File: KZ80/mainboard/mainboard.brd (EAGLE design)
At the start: 100 x 80 mm, 32 parts, among them J1 RESET, J2 PWR/CLK

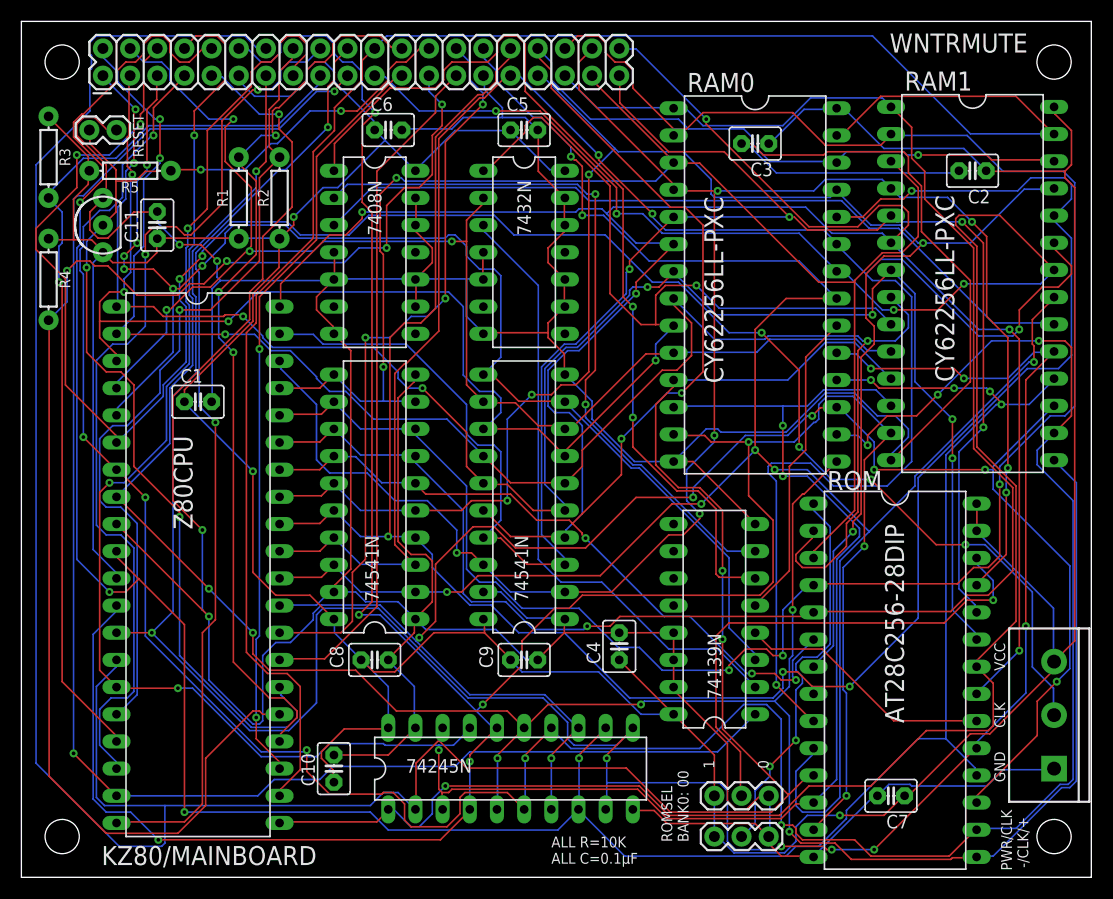
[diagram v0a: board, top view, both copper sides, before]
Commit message: mainboard: move RAM around
This moves the RAM chips to give more clearance to the ROM chip, e.g
to make swappung it out easier.
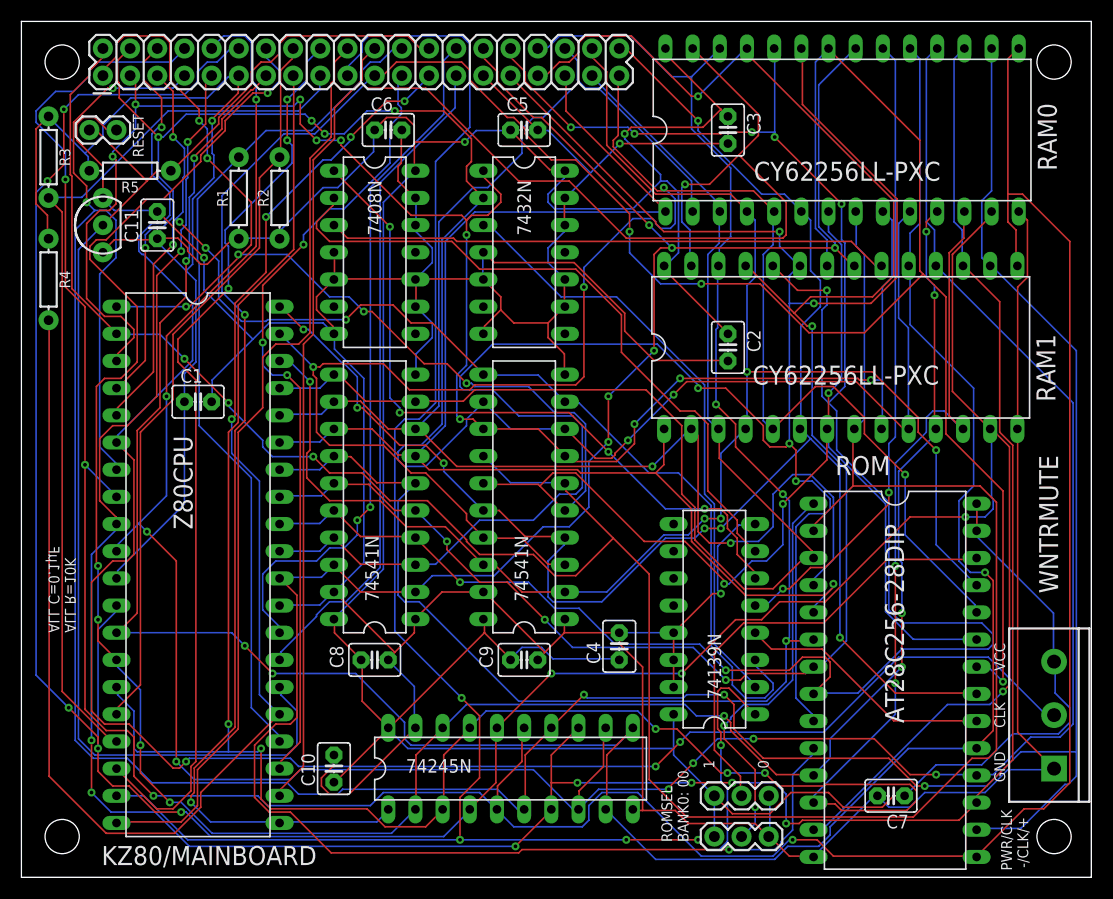
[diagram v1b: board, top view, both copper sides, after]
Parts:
- moved C2 28.2 mm to (66.0, 49.5), turned to 270 degrees
- moved RAM0 16.6 mm to (76.7, 69.8), turned to 0 degrees
- moved RAM1 13.7 mm to (76.6, 49.5), turned to 0 degrees
- moved C3 2.84 mm to (66.0, 69.8), turned to 270 degrees
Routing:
- net A12: track 159.5 -> 233.1 mm, vias 4 -> 3
- net A14: track 130.2 -> 184.2 mm, vias 4 -> 7
- net D0: track 268.7 -> 218.8 mm, vias 2 -> 10
- net A10: track 205.6 -> 156.8 mm, vias 5 -> 7
- net A6: track 187.6 -> 141.3 mm, vias 3 -> 2
- net D3: track 232.2 -> 275.2 mm, vias 7 -> 4
- net RD: track 214.0 -> 256.2 mm
- net GND: track 472.0 -> 431.0 mm, vias 2 -> 3
- net D4: track 253.0 -> 292.7 mm, vias 9 -> 5
- net A5: track 166.0 -> 128.6 mm
- net N$5: track 29.3 -> 59.8 mm, vias 0 -> 2
- net A11: track 169.3 -> 195.1 mm, vias 8 -> 9
- net MREQ: track 150.8 -> 175.0 mm, vias 2 -> 5
- net A4: track 174.6 -> 151.0 mm, vias 6 -> 3
- net A8: track 171.9 -> 150.2 mm, vias 7 -> 5
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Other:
- board text added: "REV3/20191004"
- board text removed: "REV2/20190829"
